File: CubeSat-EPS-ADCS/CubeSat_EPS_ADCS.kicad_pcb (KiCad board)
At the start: 2 copper layers, 92 x 92 mm, 22 parts, among them J1 Conn_01x02_Pin, J2 Conn_01x03_Pin, J3 Conn_01x08_Pin, J4 Screw_Terminal_01x02, J5 Screw_Terminal_01x02, J6 Screw_Terminal_01x02, J7 Screw_Terminal_01x02, J8 Screw_Terminal_01x02, U1 DRV8833 Module, U2 DRV8833 Module, U3 Buck_XL4015, U4 Buck_LM2596

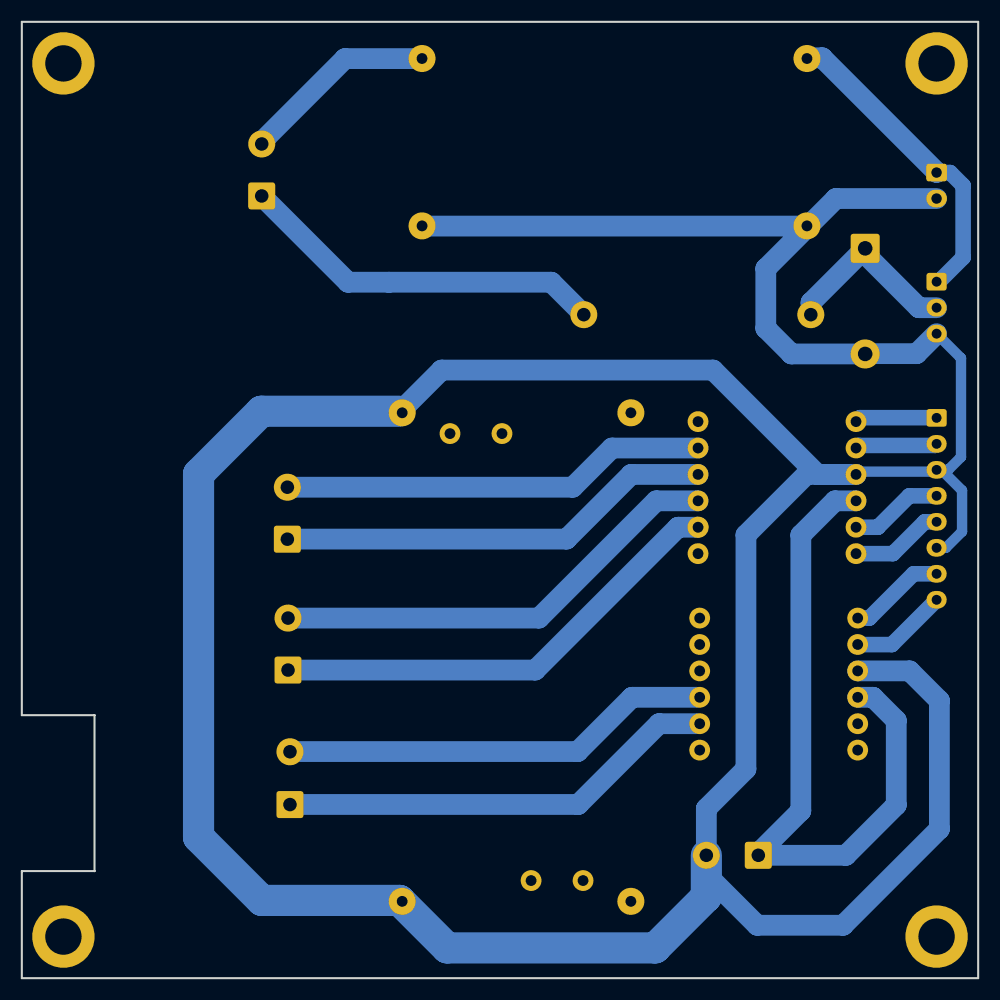
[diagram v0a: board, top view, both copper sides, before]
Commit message: changing the size of the vias
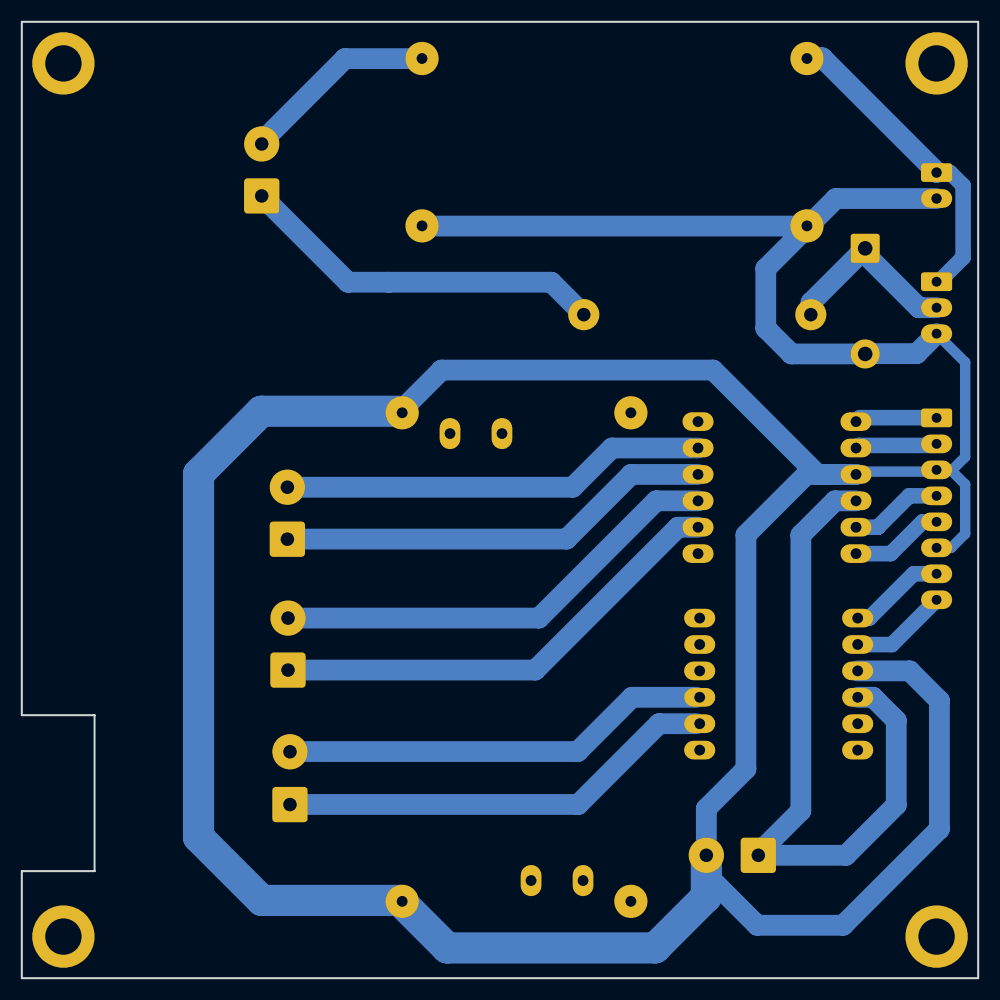
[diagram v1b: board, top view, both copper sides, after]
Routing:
- net GND: track 376.6 -> 378.2 mm
